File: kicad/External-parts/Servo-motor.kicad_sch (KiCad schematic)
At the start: 1 part, among them M2 Motor_Servo

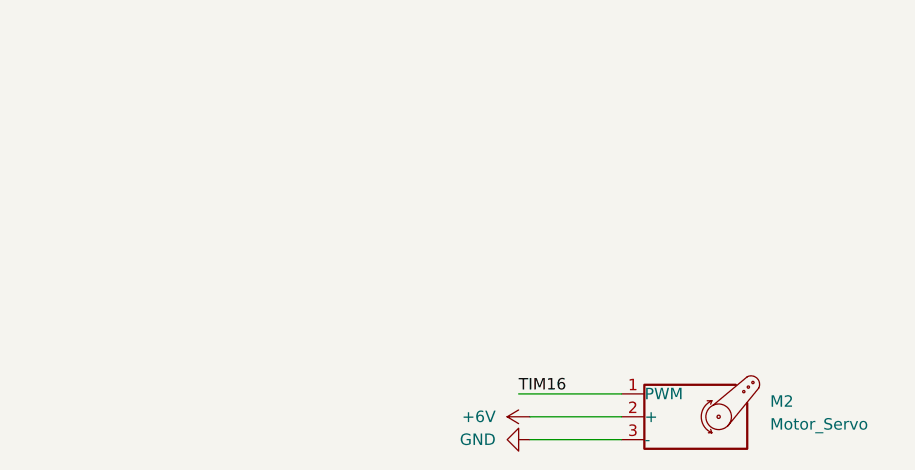
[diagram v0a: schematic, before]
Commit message: add ultrasonic, speaker, nhd
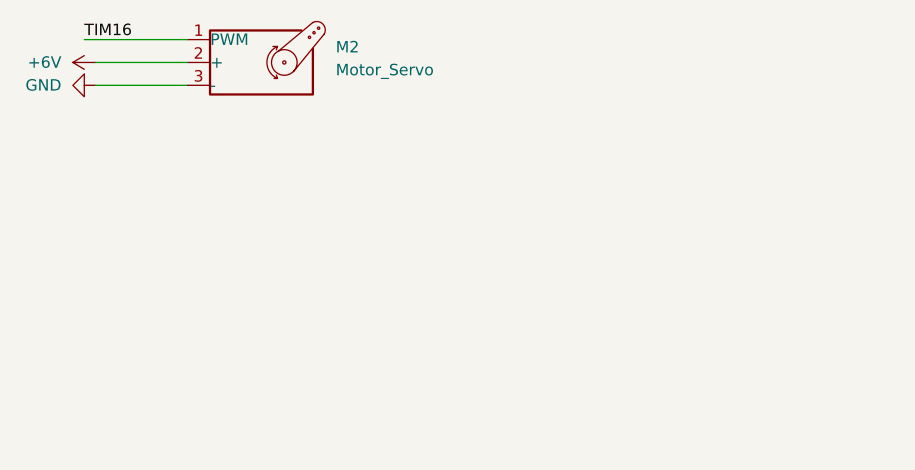
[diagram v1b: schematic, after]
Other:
- company: (none) -> ECE 47700 Team 01
- title: (none) -> Offboard 8-Ohm Speaker
- moved on the sheet: M2
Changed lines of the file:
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@@
 	(generator "eeschema")
 	(generator_version "8.0")
-	(paper "A4")
+	(paper "User" 177.8 127)
+	(title_block
+		(title "Offboard 8-Ohm Speaker")
+		(company "ECE 47700 Team 01")
+	)
 	(wire
 		(pts
-			(xy 127 92.71) (xy 137.16 92.71)
+			(xy 78.74 53.34) (xy 88.9 53.34)
 		)
 		(stroke
@@
 	(wire
 		(pts
-			(xy 127 95.25) (xy 137.16 95.25)
+			(xy 78.74 55.88) (xy 88.9 55.88)
 		)
 		(stroke
@@
 	(wire
 		(pts
-			(xy 125.73 90.17) (xy 137.16 90.17)
+			(xy 77.47 50.8) (xy 88.9 50.8)
 		)
 		(stroke
@@
 	)
 	(label "TIM16"
-		(at 125.73 90.17 0)
+		(at 77.47 50.8 0)
 		(effects
 			(font
@@
 	(symbol
 		(lib_id "Motor:Motor_Servo")
-		(at 144.78 92.71 0)
+		(at 96.52 53.34 0)
 		(unit 1)
 		(exclude_from_sim no)
@@
 		(fields_autoplaced yes)
 		(property "Reference" "M2"
-			(at 153.67 91.0065 0)
+			(at 105.41 51.6365 0)
 			(effects
 				(font
@@
 		)
 		(property "Value" "Motor_Servo"
-			(at 153.67 93.5465 0)
+			(at 105.41 54.1765 0)
 			(effects
 				(font
@@
 		)
 		(property "Footprint" ""
-			(at 144.78 97.536 0)
+			(at 96.52 58.166 0)
 			(effects
 				(font
@@
 		)
 		(property "Datasheet" "http://forums.parallax.com/uploads/attachments/46831/74481.png"
-			(at 144.78 97.536 0)
+			(at 96.52 58.166 0)
 			(effects
 				(font
@@
 		)
 		(property "Description" "Servo Motor (Futaba, HiTec, JR connector)"
-			(at 144.78 92.71 0)
+			(at 96.52 53.34 0)
 			(effects
 				(font
@@
 	(symbol
 		(lib_id "power:GND")
-		(at 127 95.25 270)
+		(at 78.74 55.88 270)
 		(unit 1)
 		(exclude_from_sim no)
@@
 		(fields_autoplaced yes)
 		(property "Reference" "#PWR02"
-			(at 120.65 95.25 0)
+			(at 72.39 55.88 0)
 			(effects
 				(font
@@
 		)
 		(property "Value" "GND"
-			(at 123.19 95.2499 90)
+			(at 74.93 55.8799 90)
 			(effects
 				(font
@@
 		)
 		(property "Footprint" ""
-			(at 127 95.25 0)
+			(at 78.74 55.88 0)
 			(effects
 				(font
@@
 		)
 		(property "Datasheet" ""
-			(at 127 95.25 0)
+			(at 78.74 55.88 0)
 			(effects
 				(font
@@
 		)
 		(property "Description" "Power symbol creates a global label with name \"GND\" , ground"
-			(at 127 95.25 0)
+			(at 78.74 55.88 0)
 			(effects
 				(font
@@
 	(symbol
 		(lib_id "power:+6V")
-		(at 127 92.71 90)
+		(at 78.74 53.34 90)
 		(unit 1)
 		(exclude_from_sim no)
@@
 		(fields_autoplaced yes)
 		(property "Reference" "#PWR01"
-			(at 130.81 92.71 0)
+			(at 82.55 53.34 0)
 			(effects
 				(font
@@
 		)
 		(property "Value" "+6V"
-			(at 123.19 92.7099 90)
+			(at 74.93 53.3399 90)
 			(effects
 				(font
@@
 		)
 		(property "Footprint" ""
-			(at 127 92.71 0)
+			(at 78.74 53.34 0)
 			(effects
 				(font
@@
 		)
 		(property "Datasheet" ""
-			(at 127 92.71 0)
+			(at 78.74 53.34 0)
 			(effects
 				(font
@@
 		)
 		(property "Description" "Power symbol creates a global label with name \"+6V\""
-			(at 127 92.71 0)
-			(effects
-				(font
+			(at 78.74 53.34 0)
+			(effects
+				(font
